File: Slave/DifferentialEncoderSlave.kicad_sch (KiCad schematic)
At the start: 32 parts, among them J1 Main, J3 Thermistor, U1 ADM4852, U2 STM32G4A1KEU4, U3 LP5907MFX-3.3, U4 MA730

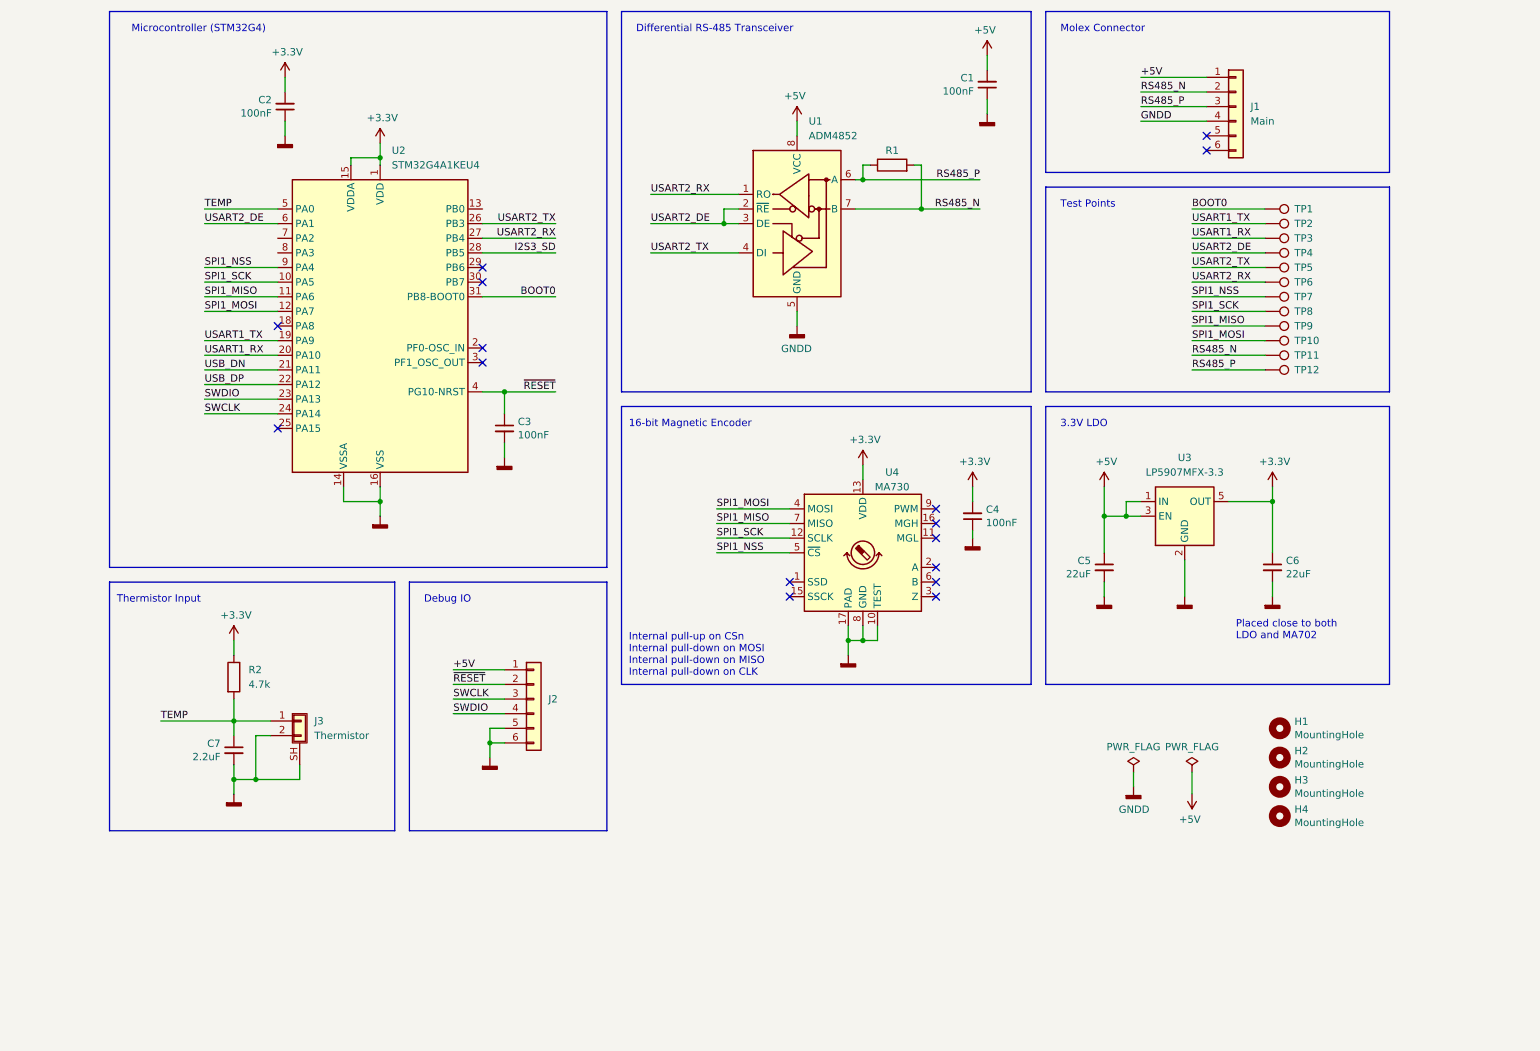
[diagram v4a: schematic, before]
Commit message: Ground CLIK-Mate shield pins
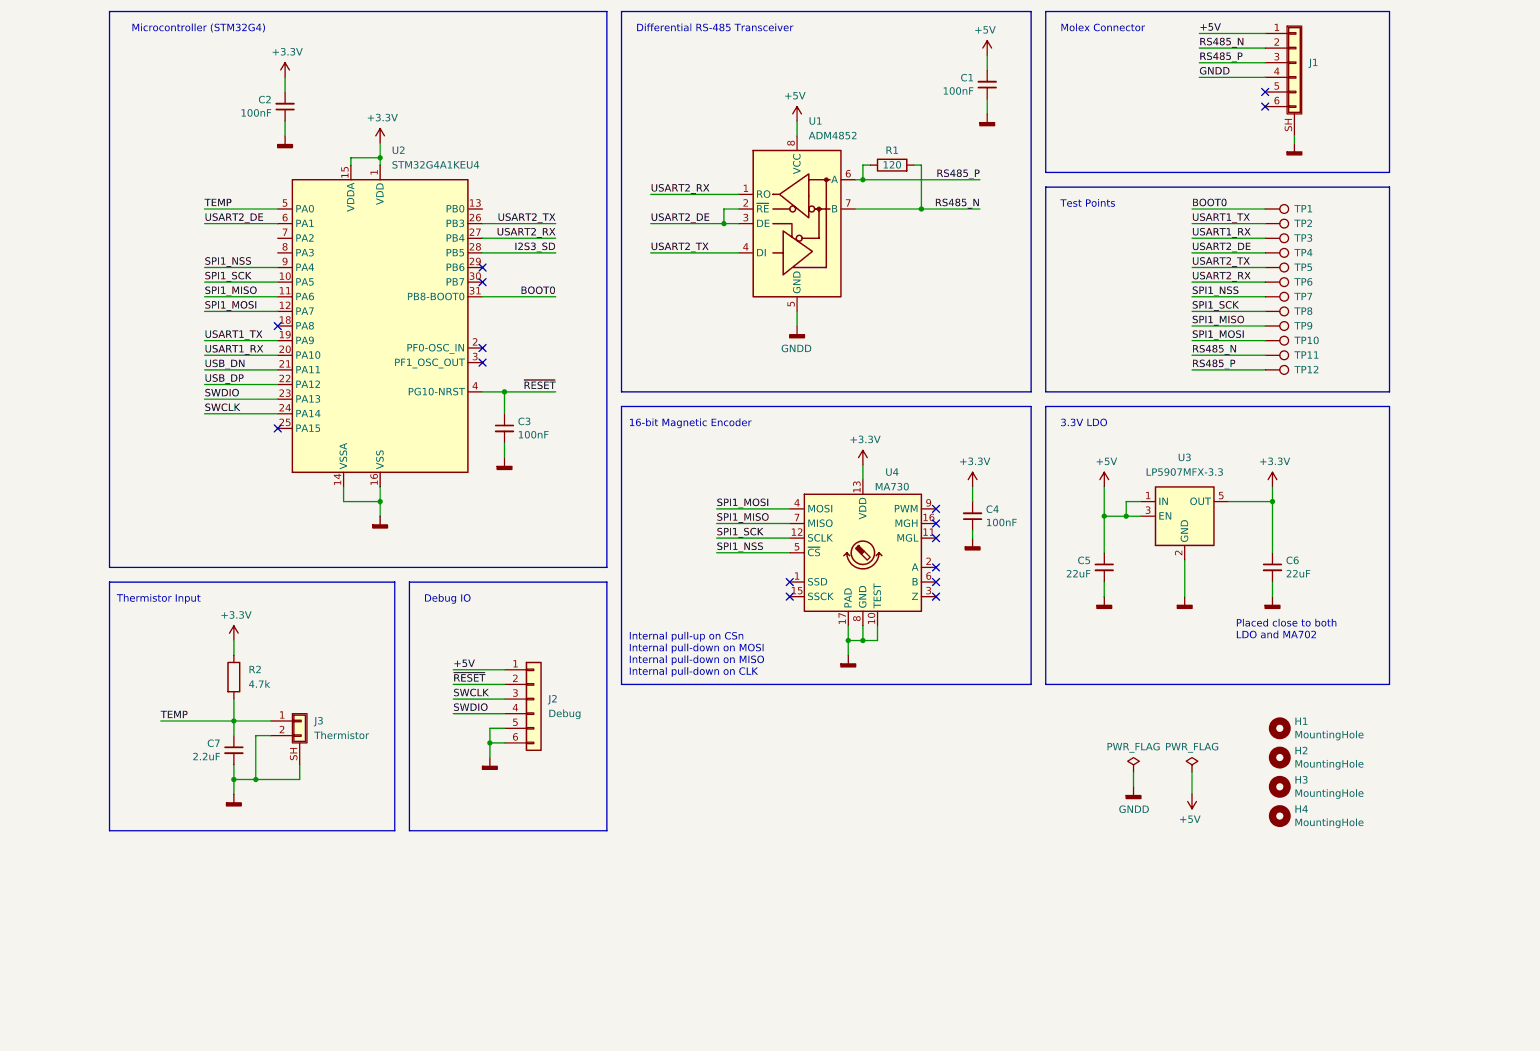
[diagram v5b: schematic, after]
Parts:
- removed J1: Main, Connector_Molex:Molex_CLIK-Mate_502585-0670_1x06-1MP_P1.50mm_Horizontal, symbol Connector_Generic:Conn_01x06
- added J1: (no value), symbol Connector_Generic_Shielded:Conn_01x06_Shielded
- J2: value (none) -> Debug
- R1: value (none) -> 120
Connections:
- net +5V: now also J1.1 (Pin_1)
- net GNDD: now also J1.4 (Pin_4), J1.SH (Shield)
- net RS485_N: now also J1.2 (Pin_2)
- net RS485_P: now also J1.3 (Pin_3)
